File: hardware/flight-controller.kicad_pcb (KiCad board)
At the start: 4 copper layers, 70 x 70 mm, 117 parts, among them J1 USB_C_Receptacle_USB2.0_16P, J10 Screw_Terminal_01x02, J11 Micro_SD_Card_Det_Hirose_DM3AT, J12 Conn_01x03, J13 Conn_01x03, J14 Conn_01x03, J15 Conn_01x03, J16 Screw_Terminal_01x02, J17 Conn_01x04, J18 Screw_Terminal_01x02, J19 Conn_01x02, J2 Conn_01x02, J20 Conn_01x02, J21 Conn_01x02, J22 Conn_01x02, J23 Conn_01x02, J3 Conn_Coaxial, J4 Conn_01x04, J5 Screw_Terminal_01x02, J6 Conn_01x04, J7 Screw_Terminal_01x02, J8 Conn_01x04, J9 Screw_Terminal_01x02, U1 BMP384, U2 LSM6DSOTR, U3 MMC5983MA, U4 NEO-M9N, U5 TPS2121RUXR, U6 AP62300TWU, U7 STM32H723VGTx, Y1 Q13FC13500004, Y2 X322525MOB4SI

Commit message: updated silkscreen
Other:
- board text added: "BL"
- board text added: "BR"
- board text added: "ESC"
- board text added: "FL"
- board text added: "FR"
- board text removed: "PWM"
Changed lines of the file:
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@@
+		)
+	)
+	(gr_text "BL"
+		(at 129.68 127.96 0)
+		(layer "F.SilkS")
+		(effects
+			(font
+				(size 1 1)
+				(thickness 0.15)
+			)
 		)
 	)
@@
 				(size 1.5 1.5)
 				(thickness 0.1875)
+			)
+		)
+	)
+	(gr_text "FR"
+		(at 125.09 127.96 0)
+		(layer "F.SilkS")
+		(effects
+			(font
+				(size 1 1)
+				(thickness 0.15)
+			)
+		)
+	)
+	(gr_text "BR"
+		(at 134.27 127.96 0)
+		(layer "F.SilkS")
+		(effects
+			(font
+				(size 1 1)
+				(thickness 0.15)
+			)
+		)
+	)
+	(gr_text "FL"
+		(at 120.5 127.96 0)
+		(layer "F.SilkS")
+		(effects
+			(font
+				(size 1 1)
+				(thickness 0.15)
 			)
 		)
@@
 		)
 	)
-	(gr_text "PWM"
-		(at 127.5 127.5 0)
+	(gr_text "ESC"
+		(at 127.5 126 0)
 		(layer "F.SilkS")
 		(effects

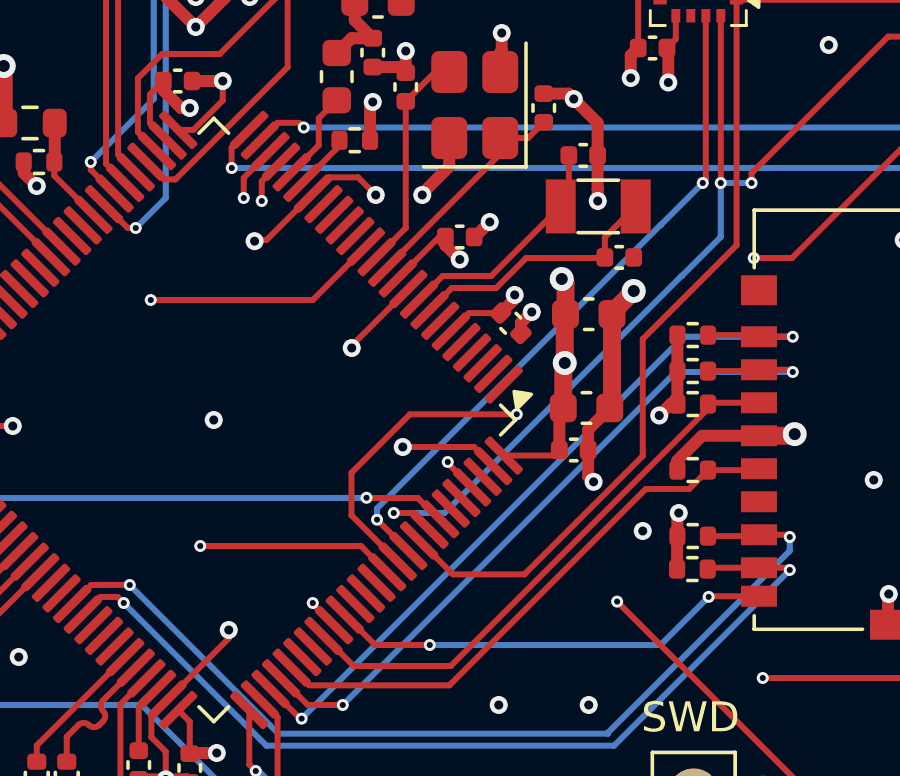
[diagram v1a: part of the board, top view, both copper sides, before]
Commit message: changed int pins and fixed i2c
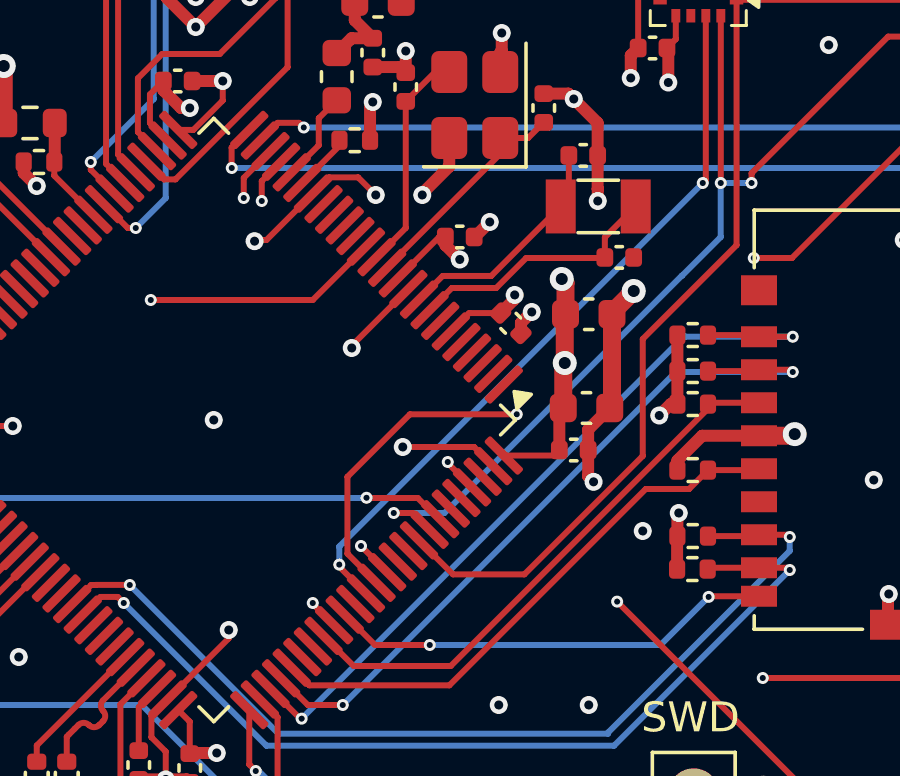
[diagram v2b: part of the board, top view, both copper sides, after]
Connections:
- U7 pad 87: unconnected-(U7-PD6-Pad87) -> /MMC_INT
- U7 pad 88: unconnected-(U7-PD7-Pad88) -> /BMP_INT
- U7 pad 90: /BMP_INT -> unconnected-(U7-PB4(NJTRST)-Pad90)
- U7 pad 91: /MMC_INT -> unconnected-(U7-PB5-Pad91)
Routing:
- net /MMC_INT: track 22.8 -> 24.7 mm
- net /BMP_INT: track 29.9 -> 30.4 mm

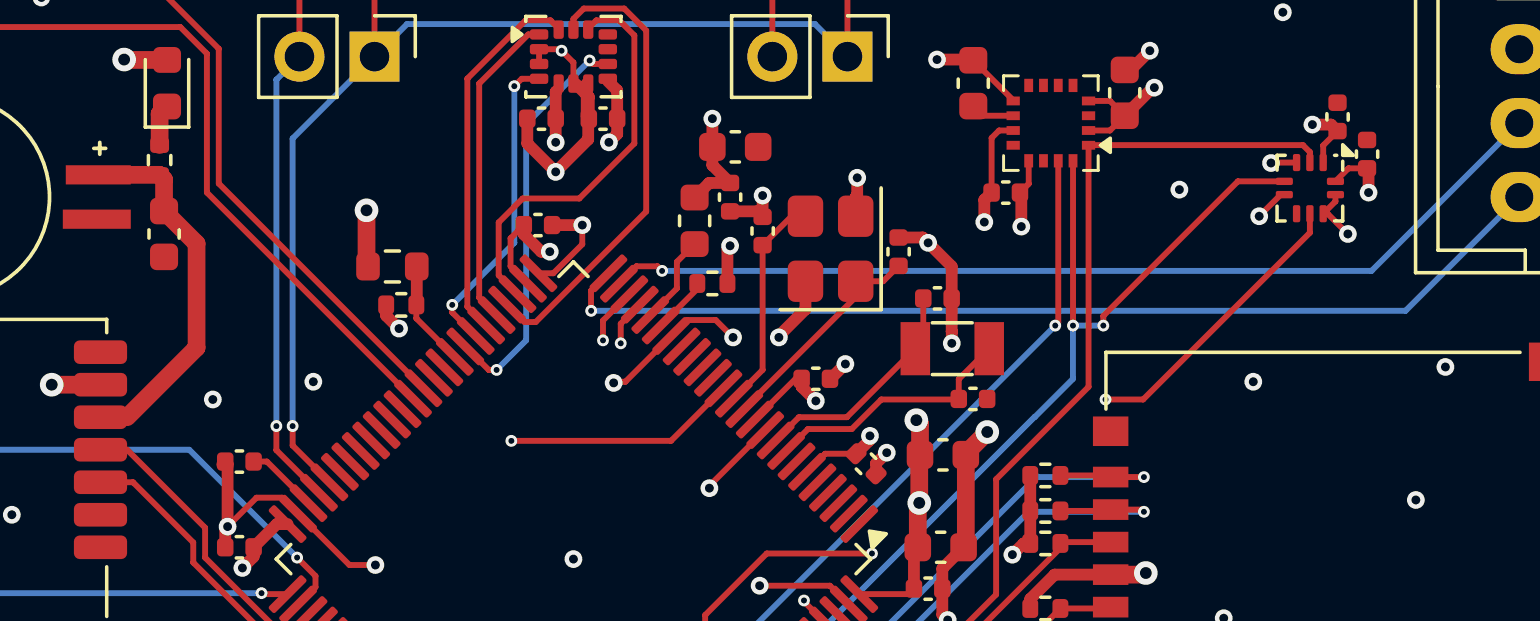
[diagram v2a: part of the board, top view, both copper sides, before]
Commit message: added i2c pullup resistors
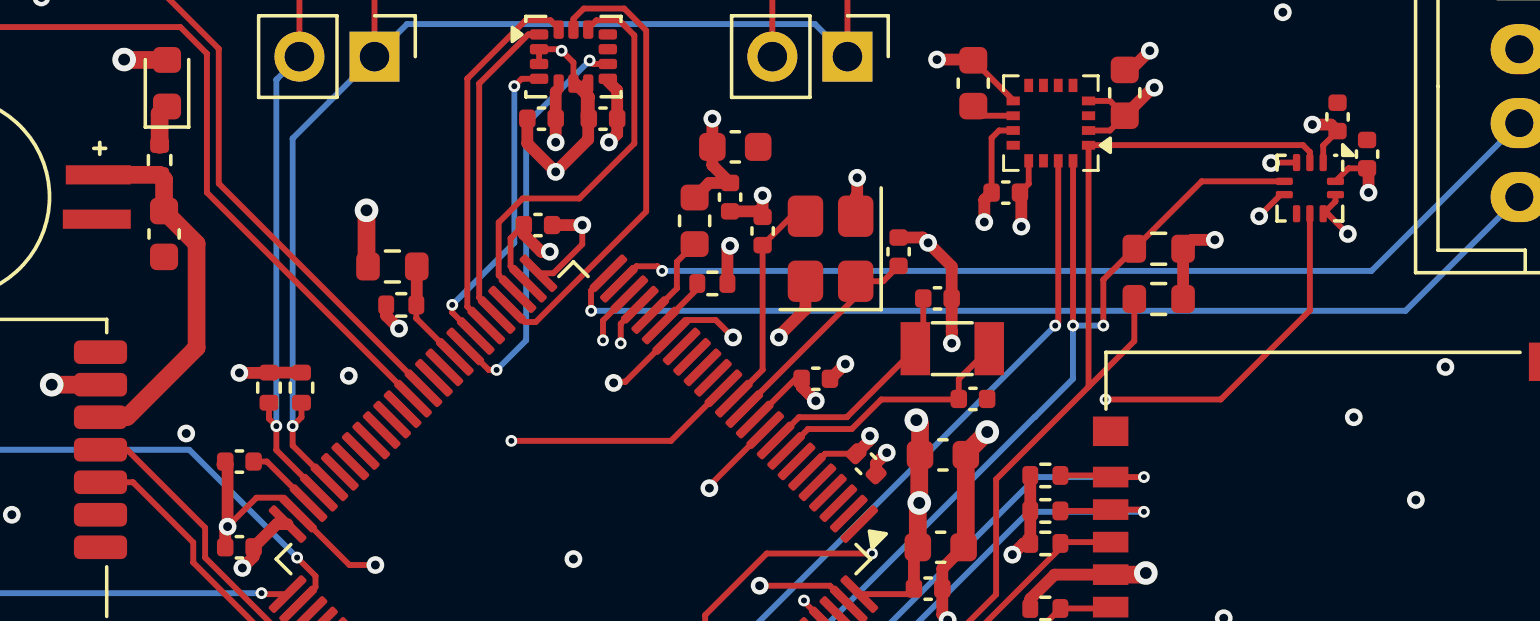
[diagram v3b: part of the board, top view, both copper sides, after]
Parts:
- added R31: 1.2K, Resistor_SMD:R_0603_1608Metric, F.Cu at (161.8, 94.2)
- added R32: 1.2K, Resistor_SMD:R_0603_1608Metric, F.Cu at (161.8, 92.5)
- added R33: 4.7K, Resistor_SMD:R_0402_1005Metric, F.Cu at (132.8, 97.2)
- added R34: 4.7K, Resistor_SMD:R_0402_1005Metric, F.Cu at (131.7, 97.2)
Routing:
- net +3.3V: track 82.0 -> 87.0 mm, vias 23 -> 25
- net /SCL1: track 34.0 -> 37.6 mm
- net /BMP_INT: track 30.4 -> 31.9 mm
- net /SCL2: track 42.2 -> 43.1 mm
- net /SDA2: track 42.9 -> 43.8 mm
- net /SDA1: track 32.9 -> 33.6 mm
- net GND: vias 187 -> 186
